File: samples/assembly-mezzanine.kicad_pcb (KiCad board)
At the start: 2 copper layers, 9.5 x 11.2 mm, 2 parts

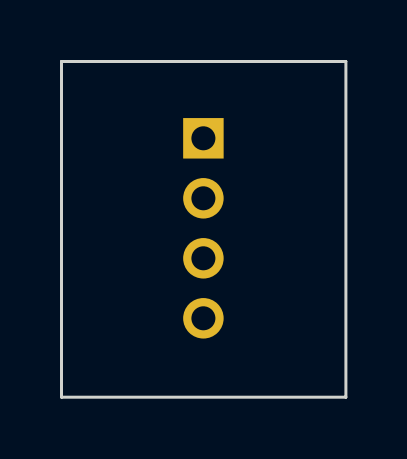
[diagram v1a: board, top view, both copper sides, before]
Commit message: Update assembly coupler samples
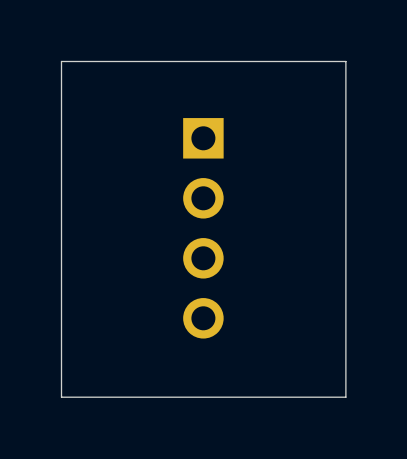
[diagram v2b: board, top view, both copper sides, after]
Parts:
- mezzanine: footprint Kikakuka:CouplerMoving -> PCM_Kikakuka:CouplerMoving
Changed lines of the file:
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@@
 		)
 	)
-	(footprint "Kikakuka:CouplerMoving"
+	(footprint "PCM_Kikakuka:CouplerMoving"
 		(layer "B.Cu")
 		(at 142.97 96.42 180)
@@
 			)
 		)
-		(property "Description" ""
+		(property "Description" "Moving FreekiCAD alignment plane. Positions this PCB against a CouplerFixed footprint with the same reference. Z moves along the PCB surface normal; positive Offset moves on the PCB surface in the triangle direction; Tilt rotates around local X. Unitless lengths default to mm; mm/in/mil/um are supported."
 			(at 0 0 0)
 			(unlocked yes)
@@
 			)
 		)
-		(property "Z" "2mm"
+		(property "Z" "2 mm"
 			(at 0 0 0)
 			(unlocked yes)
@@
 		)
 		(fp_line
+			(start 0.25 0.75)
+			(end 0 0.5)
+			(stroke
+				(width 0.1)
+				(type default)
+			)
+			(layer "Cmts.User")
+		)
+		(fp_line
+			(start 0 1)
+			(end 0 0.5)
+			(stroke
+				(width 0.1)
+				(type default)
+			)
+			(layer "Cmts.User")
+		)
+		(fp_line
+			(start 0 0.5)
+			(end -0.25 0.75)
+			(stroke
+				(width 0.1)
+				(type default)
+			)
+			(layer "Cmts.User")
+		)
+		(fp_line
 			(start 0 0)
 			(end -1 1)
+			(stroke
+				(width 0.1)
+				(type default)
+			)
+			(layer "Cmts.User")
+		)
+		(fp_line
+			(start -0.25 0.75)
+			(end 0 0.5)
 			(stroke
 				(width 0.1)
@@
 		(embedded_fonts no)
 	)
-	(gr_rect
+	(gr_line
 		(start 138.24 93.86)
+		(end 138.24 105.05)
+		(stroke
+			(width 0)
+			(type default)
+		)
+		(layer "Edge.Cuts")
+	)
+	(gr_line
+		(start 138.24 105.05)
 		(end 147.72 105.05)
 		(stroke
-			(width 0.1)
+			(width 0)
 			(type default)
 		)
-		(fill no)
 		(layer "Edge.Cuts")
 	)
+	(gr_line
+		(start 147.72 93.86)
+		(end 138.24 93.86)
+		(stroke
+			(width 0)
+			(type default)
+		)
+		(layer "Edge.Cuts")
+	)
+	(gr_line
+		(start 147.72 105.05)
+		(end 147.72 93.86)
+		(stroke
+			(width 0)
+			(type default)
+		)
+		(layer "Edge.Cuts")
+	)
